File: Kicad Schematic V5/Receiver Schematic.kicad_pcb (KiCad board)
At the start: 2 copper layers, 95.3 x 95.2 mm, 56 parts, among them J1 SJ1-3525N, U1 Pico, U2 Si5351A-B-GT, U3 SN74CBT3253, U4 LM2904, Y1 CX3225SB 25MHz

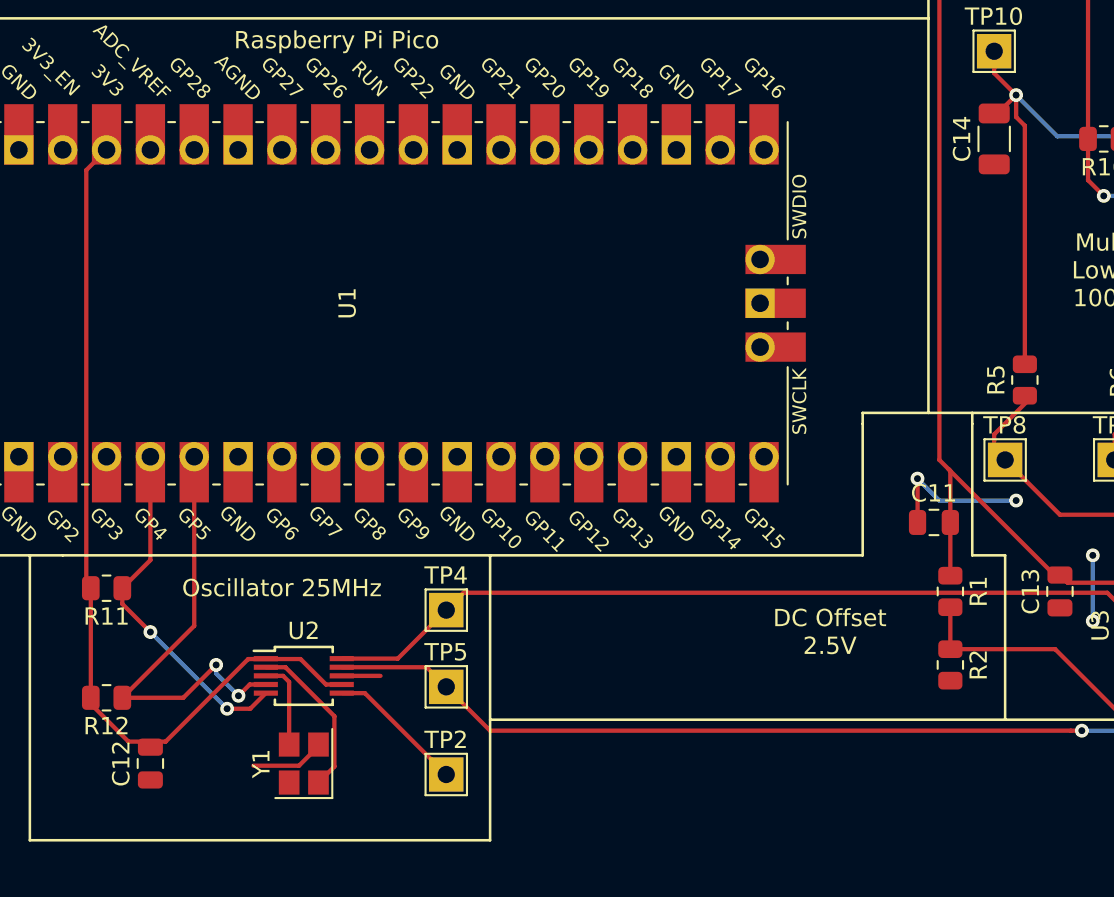
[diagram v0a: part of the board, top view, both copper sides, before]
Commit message: Version 5
Updated File organization and minor fixes.
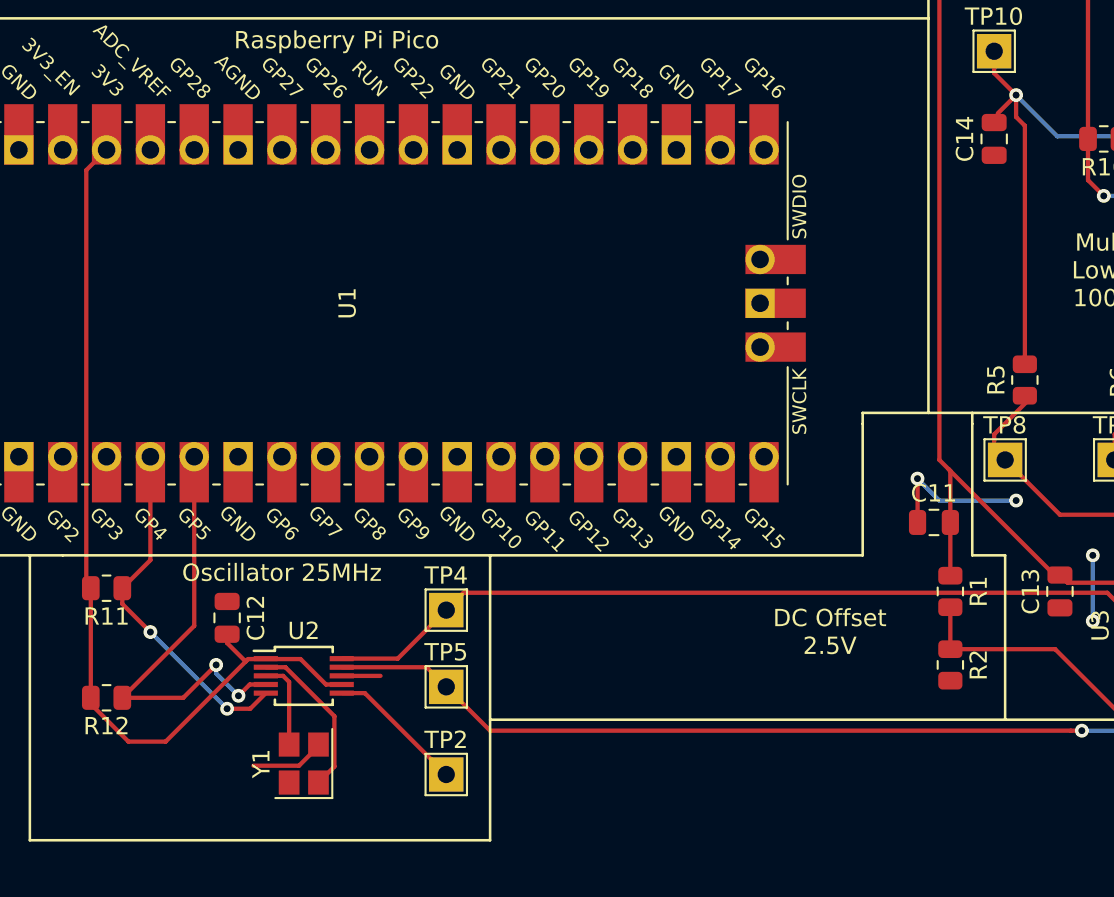
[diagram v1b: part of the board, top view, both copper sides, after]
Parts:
- C14: footprint Capacitor_SMD:C_1206_3216Metric -> Capacitor_SMD:C_0805_2012Metric
- U4: value LM2904 -> LM4562MA
- moved C12 9.54 mm to (71.1, 102.7), turned to -90 degrees
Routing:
- net +3V3: track 50.7 -> 52.8 mm
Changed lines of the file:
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@@
   )
   (footprint "Capacitor_SMD:C_0805_2012Metric" (layer "F.Cu")
-    (at 66.675 111.125 90)
+    (at 71.12 102.682 -90)
     (descr "Capacitor SMD 0805 (2012 Metric), square (rectangular) end terminal, IPC_7351 nominal, (Body size source: IPC-SM-782 page 76, https://www.pcb-3d.com/wordpress/wp-content/uploads/ipc-sm-782a_amendment_1_and_2.pdf, https://docs.google.com/spreadsheets/d/1BsfQQcO9C6DZCsRaXUlFlo91Tg2WpOkGARC1WS5S8t0/edit?usp=sharing), generated with kicad-footprint-generator")
     (tags "capacitor")
@@
     (fp_line (start 1 -0.625) (end 1 0.625) (layer "F.Fab") (width 0.1))
     (fp_line (start -1 0.625) (end -1 -0.625) (layer "F.Fab") (width 0.1))
-    (pad "1" smd roundrect (at -0.95 0 90) (size 1 1.45) (layers "F.Cu" "F.Paste" "F.Mask") (roundrect_rratio 0.25)
+    (pad "1" smd roundrect (at -0.95 0 270) (size 1 1.45) (layers "F.Cu" "F.Paste" "F.Mask") (roundrect_rratio 0.25)
       (net 1 "GND") (pintype "passive"))
-    (pad "2" smd roundrect (at 0.95 0 90) (size 1 1.45) (layers "F.Cu" "F.Paste" "F.Mask") (roundrect_rratio 0.25)
+    (pad "2" smd roundrect (at 0.95 0 270) (size 1 1.45) (layers "F.Cu" "F.Paste" "F.Mask") (roundrect_rratio 0.25)
       (net 9 "+3V3") (pintype "passive"))
     (model "${KICAD6_3DMODEL_DIR}/Capacitor_SMD.3dshapes/C_0805_2012Metric.wrl"
@@
       (effects (font (size 1 1) (thickness 0.15)))
     )
-    (fp_text value "LM2904" (at 0 3.4) (layer "F.Fab")
+    (fp_text value "LM4562MA" (at 0 3.4) (layer "F.Fab")
       (effects (font (size 1 1) (thickness 0.15)))
     )
@@
     )
   )
-  (footprint "Capacitor_SMD:C_1206_3216Metric" (layer "F.Cu")
+  (footprint "Capacitor_SMD:C_0805_2012Metric" (layer "F.Cu")
     (at 115.57 74.93 90)
-    (descr "Capacitor SMD 1206 (3216 Metric), square (rectangular) end terminal, IPC_7351 nominal, (Body size source: IPC-SM-782 page 76, https://www.pcb-3d.com/wordpress/wp-content/uploads/ipc-sm-782a_amendment_1_and_2.pdf), generated with kicad-footprint-generator")
+    (descr "Capacitor SMD 0805 (2012 Metric), square (rectangular) end terminal, IPC_7351 nominal, (Body size source: IPC-SM-782 page 76, https://www.pcb-3d.com/wordpress/wp-content/uploads/ipc-sm-782a_amendment_1_and_2.pdf, https://docs.google.com/spreadsheets/d/1BsfQQcO9C6DZCsRaXUlFlo91Tg2WpOkGARC1WS5S8t0/edit?usp=sharing), generated with kicad-footprint-generator")
     (tags "capacitor")
     (property "Sheetfile" "Receiver Schematic.kicad_sch")
     (property "Sheetname" "")
     (attr smd)
-    (fp_text reference "C14" (at 0 -1.85 90) (layer "F.SilkS")
-      (effects (font (size 1 1) (thickness 0.15)))
-    )
-    (fp_text value "7.5n" (at 0 1.85 90) (layer "F.Fab")
+    (fp_text reference "C14" (at 0 -1.68 90) (layer "F.SilkS")
+      (effects (font (size 1 1) (thickness 0.15)))
+    )
+    (fp_text value "7.5n" (at 0 1.68 90) (layer "F.Fab")
       (effects (font (size 1 1) (thickness 0.15)))
     )
     (fp_text user "${REFERENCE}" (at 0 0 90) (layer "F.Fab")
-      (effects (font (size 0.8 0.8) (thickness 0.12)))
-    )
-    (fp_line (start -0.711252 -0.91) (end 0.711252 -0.91) (layer "F.SilkS") (width 0.12))
-    (fp_line (start -0.711252 0.91) (end 0.711252 0.91) (layer "F.SilkS") (width 0.12))
-    (fp_line (start -2.3 1.15) (end -2.3 -1.15) (layer "F.CrtYd") (width 0.05))
-    (fp_line (start 2.3 -1.15) (end 2.3 1.15) (layer "F.CrtYd") (width 0.05))
-    (fp_line (start -2.3 -1.15) (end 2.3 -1.15) (layer "F.CrtYd") (width 0.05))
-    (fp_line (start 2.3 1.15) (end -2.3 1.15) (layer "F.CrtYd") (width 0.05))
-    (fp_line (start 1.6 -0.8) (end 1.6 0.8) (layer "F.Fab") (width 0.1))
-    (fp_line (start 1.6 0.8) (end -1.6 0.8) (layer "F.Fab") (width 0.1))
-    (fp_line (start -1.6 -0.8) (end 1.6 -0.8) (layer "F.Fab") (width 0.1))
-    (fp_line (start -1.6 0.8) (end -1.6 -0.8) (layer "F.Fab") (width 0.1))
-    (pad "1" smd roundrect (at -1.475 0 90) (size 1.15 1.8) (layers "F.Cu" "F.Paste" "F.Mask") (roundrect_rratio 0.2173913043)
+      (effects (font (size 0.5 0.5) (thickness 0.08)))
+    )
+    (fp_line (start -0.261252 0.735) (end 0.261252 0.735) (layer "F.SilkS") (width 0.12))
+    (fp_line (start -0.261252 -0.735) (end 0.261252 -0.735) (layer "F.SilkS") (width 0.12))
+    (fp_line (start 1.7 -0.98) (end 1.7 0.98) (layer "F.CrtYd") (width 0.05))
+    (fp_line (start 1.7 0.98) (end -1.7 0.98) (layer "F.CrtYd") (width 0.05))
+    (fp_line (start -1.7 0.98) (end -1.7 -0.98) (layer "F.CrtYd") (width 0.05))
+    (fp_line (start -1.7 -0.98) (end 1.7 -0.98) (layer "F.CrtYd") (width 0.05))
+    (fp_line (start -1 0.625) (end -1 -0.625) (layer "F.Fab") (width 0.1))
+    (fp_line (start 1 -0.625) (end 1 0.625) (layer "F.Fab") (width 0.1))
+    (fp_line (start -1 -0.625) (end 1 -0.625) (layer "F.Fab") (width 0.1))
+    (fp_line (start 1 0.625) (end -1 0.625) (layer "F.Fab") (width 0.1))
+    (pad "1" smd roundrect (at -0.95 0 90) (size 1 1.45) (layers "F.Cu" "F.Paste" "F.Mask") (roundrect_rratio 0.25)
       (net 1 "GND") (pintype "passive"))
-    (pad "2" smd roundrect (at 1.475 0 90) (size 1.15 1.8) (layers "F.Cu" "F.Paste" "F.Mask") (roundrect_rratio 0.2173913043)
+    (pad "2" smd roundrect (at 0.95 0 90) (size 1 1.45) (layers "F.Cu" "F.Paste" "F.Mask") (roundrect_rratio 0.25)
       (net 10 "Net-(C14-Pad2)") (pintype "passive"))
-    (model "${KICAD6_3DMODEL_DIR}/Capacitor_SMD.3dshapes/C_1206_3216Metric.wrl"
+    (model "${KICAD6_3DMODEL_DIR}/Capacitor_SMD.3dshapes/C_0805_2012Metric.wrl"
       (offset (xyz 0 0 0))
       (scale (xyz 1 1 1))
@@
     (effects (font (size 1 1) (thickness 0.15)))
   )
-  (gr_text "Oscillator 25MHz\n" (at 74.295 100.965) (layer "F.SilkS")
+  (gr_text "Oscillator 25MHz\n" (at 74.295 100.076) (layer "F.SilkS")
     (effects (font (size 1 1) (thickness 0.15)))
   )
@@
   (segment (start 134.835092 77.11702) (end 128.965072 71.247) (width 0.25) (layer "F.Cu") (net 8))
   (segment (start 140.335 80.435) (end 142.87 77.9) (width 0.25) (layer "F.Cu") (net 8))
+  (segment (start 72.195489 105.215489) (end 71.12 104.14) (width 0.25) (layer "F.Cu") (net 9))
   (segment (start 67.555978 109.855) (end 65.405 109.855) (width 0.25) (layer "F.Cu") (net 9))
+  (segment (start 72.195489 105.215489) (end 67.555978 109.855) (width 0.25) (layer "F.Cu") (net 9))
   (segment (start 75.375 105.070489) (end 72.340489 105.070489) (width 0.25) (layer "F.Cu") (net 9))
   (segment (start 65.405 109.855) (end 63.2225 107.6725) (width 0.25) (layer "F.Cu") (net 9))
-  (segment (start 72.340489 105.070489) (end 67.555978 109.855) (width 0.25) (layer "F.Cu") (net 9))
   (segment (start 62.960489 76.739511) (end 62.960489 100.702989) (width 0.25) (layer "F.Cu") (net 9))
   (segment (start 63.2225 107.6725) (end 63.2225 107.315) (width 0.25) (layer "F.Cu") (net 9))
   (segment (start 77.765 106.545) (end 76.849511 106.545) (width 0.25) (layer "F.Cu") (net 9))
+  (segment (start 71.12 104.14) (end 71.12 103.632) (width 0.25) (layer "F.Cu") (net 9))
   (segment (start 62.960489 100.702989) (end 63.2225 100.965) (width 0.25) (layer "F.Cu") (net 9))
+  (segment (start 72.340489 105.070489) (end 72.195489 105.215489) (width 0.25) (layer "F.Cu") (net 9))
   (segment (start 64.135 75.565) (end 62.960489 76.739511) (width 0.25) (layer "F.Cu") (net 9))
   (segment (start 63.2225 100.965) (end 63.2225 107.315) (width 0.25) (layer "F.Cu") (net 9))
